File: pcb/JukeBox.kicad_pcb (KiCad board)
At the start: 2 copper layers, 102 x 100 mm, 102 parts, among them J1 USB_C_Receptacle_USB2.0_16P, Q1 Q_NPN_BEC, SW1 SW_SPST, SW10 SW_SPST, SW11 SW_SPST, SW12 SW_SPST, SW2 SW_SPST, SW3 SW_SPST, SW4 SW_SPST, SW5 SW_SPST, SW6 SW_SPST, SW7 SW_SPST, SW8 SW_SPST, SW9 SW_SPST, U1 NCP1117-3.3_SOT223, U2 W25Q128JVS, U3 RP2350_60QFN, U5 CAT24C512, Y2 ABM8-272-T3

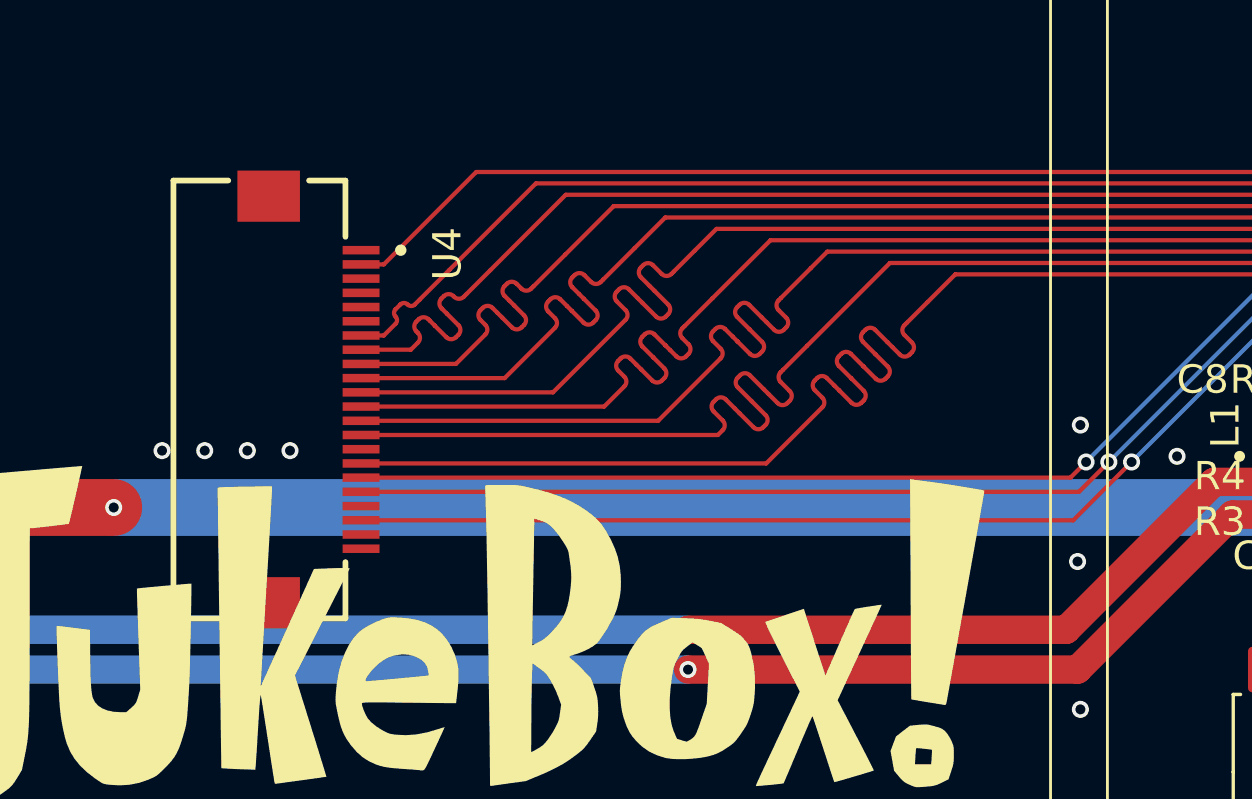
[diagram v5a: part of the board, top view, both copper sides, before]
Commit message: update to new part on pcb for screen
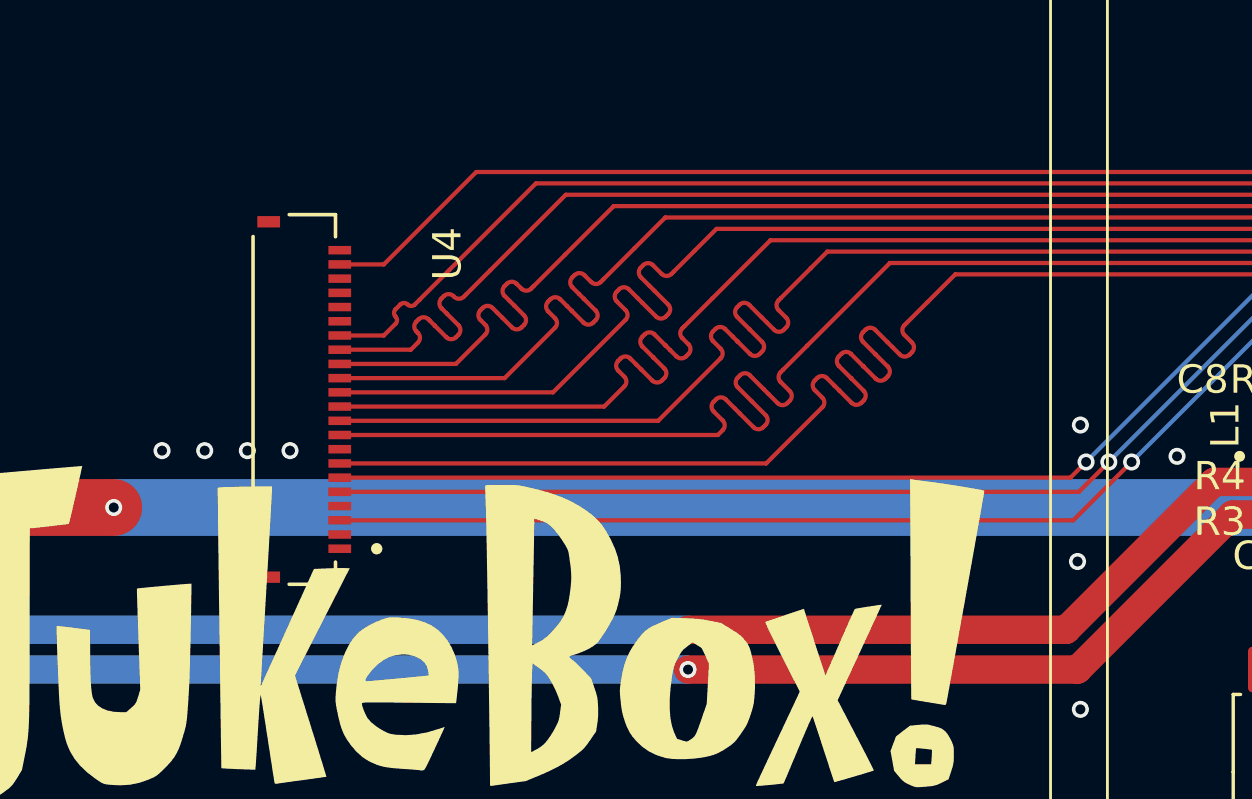
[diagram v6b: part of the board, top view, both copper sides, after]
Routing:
- net /SCRD3: track 54.9 -> 55.7 mm
- net /SCRRST: track 64.9 -> 65.7 mm
- net /SCRDC: track 66.4 -> 67.2 mm
- net /SCRD7: track 55.0 -> 55.7 mm
- net /SCRD6: track 54.9 -> 55.7 mm
- net /SCRD5: track 54.9 -> 55.7 mm
- net /SCRD2: track 54.9 -> 55.7 mm
- net /SCRD1: track 54.9 -> 55.7 mm
- net /SCRD0: track 54.9 -> 55.7 mm
- net /SCRCS: track 66.9 -> 67.7 mm
- net /SCRCLK: track 54.9 -> 55.6 mm
- net /LEDK: track 55.5 -> 56.2 mm
- net /SCRD4: track 54.9 -> 55.7 mm

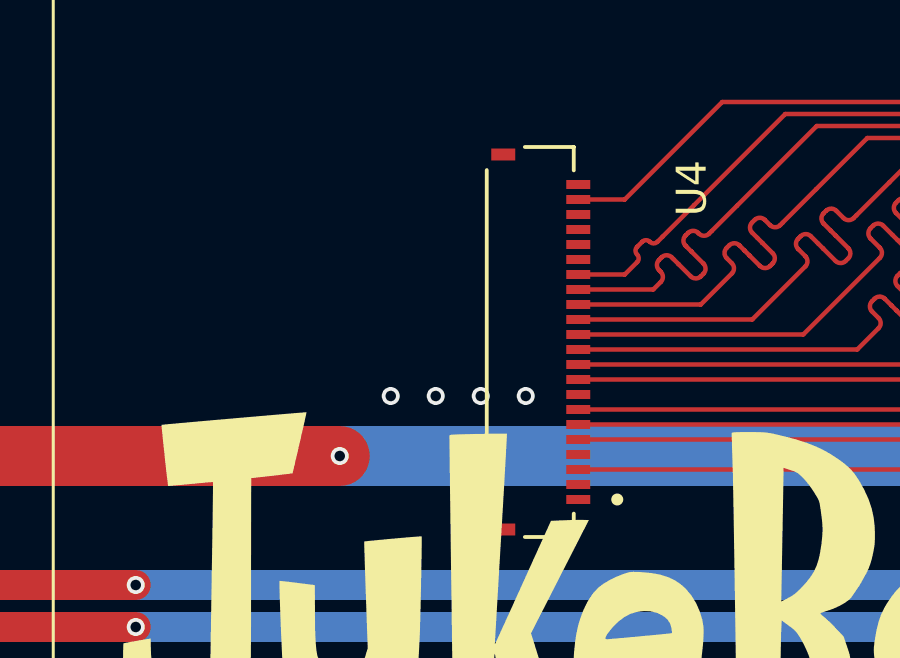
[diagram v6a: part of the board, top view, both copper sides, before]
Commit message: finalize power rails for new screen
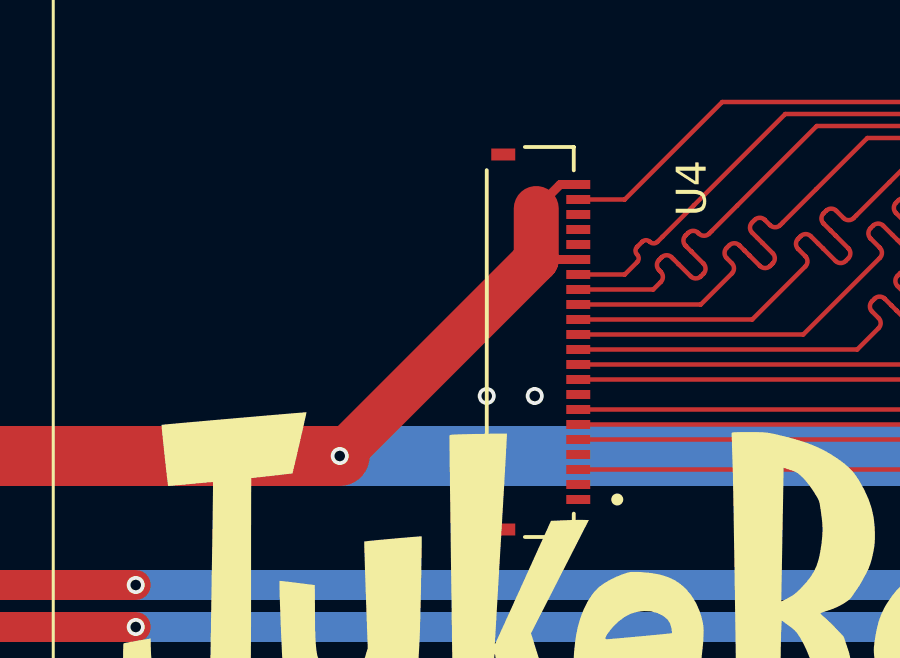
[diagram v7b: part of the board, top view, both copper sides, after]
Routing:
- net +3V3: track 149.5 -> 163.6 mm
- net GND: vias 57 -> 55
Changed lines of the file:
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@@
 	)
 	(via
-		(at 107.09 85.5)
+		(at 107.39 85.5)
 		(size 0.6)
 		(drill 0.35)
@@
 	)
 	(via
-		(at 102.59 85.5)
-		(size 0.6)
-		(drill 0.35)
-		(layers "F.Cu" "B.Cu")
-		(free yes)
-		(net 1)
-	)
-	(via
 		(at 155.19 84.6)
 		(size 0.6)
@@
 	)
 	(via
-		(at 104.09 85.5)
-		(size 0.6)
-		(drill 0.35)
-		(layers "F.Cu" "B.Cu")
-		(free yes)
-		(net 1)
-	)
-	(via
 		(at 148.09 79.5)
 		(size 0.6)
@@
 	)
 	(via
-		(at 105.59 85.5)
+		(at 105.79 85.5)
 		(size 0.6)
 		(drill 0.35)
@@
 	)
 	(segment
+		(start 108.24 78.45)
+		(end 108.84 78.45)
+		(width 0.3)
+		(layer "F.Cu")
+		(net 5)
+	)
+	(segment
+		(start 107.44 80.95)
+		(end 107.74 80.95)
+		(width 0.15)
+		(layer "F.Cu")
+		(net 5)
+	)
+	(segment
 		(start 144.27 88)
 		(end 144.47 88.2)
@@
 		(end 153.6275 85)
 		(width 0.15)
+		(layer "F.Cu")
+		(net 5)
+	)
+	(segment
+		(start 108.84 80.95)
+		(end 107.74 80.95)
+		(width 0.3)
 		(layer "F.Cu")
 		(net 5)
@@
 	)
 	(segment
+		(start 107.44 79.25)
+		(end 108.24 78.45)
+		(width 0.3)
+		(layer "F.Cu")
+		(net 5)
+	)
+	(segment
 		(start 150.19 84.3625)
 		(end 150.19 85)
@@
 	)
 	(segment
+		(start 100.89 87.5)
+		(end 107.44 80.95)
+		(width 1.5)
+		(layer "F.Cu")
+		(net 5)
+	)
+	(segment
 		(start 75.89 94.7)
 		(end 78.26 94.7)
@@
 		(layer "F.Cu")
 		(net 5)
+	)
+	(segment
+		(start 107.44 80.95)
+		(end 107.44 79.25)
+		(width 1.5)
+		(layer "F.Cu")
+		(net 5)

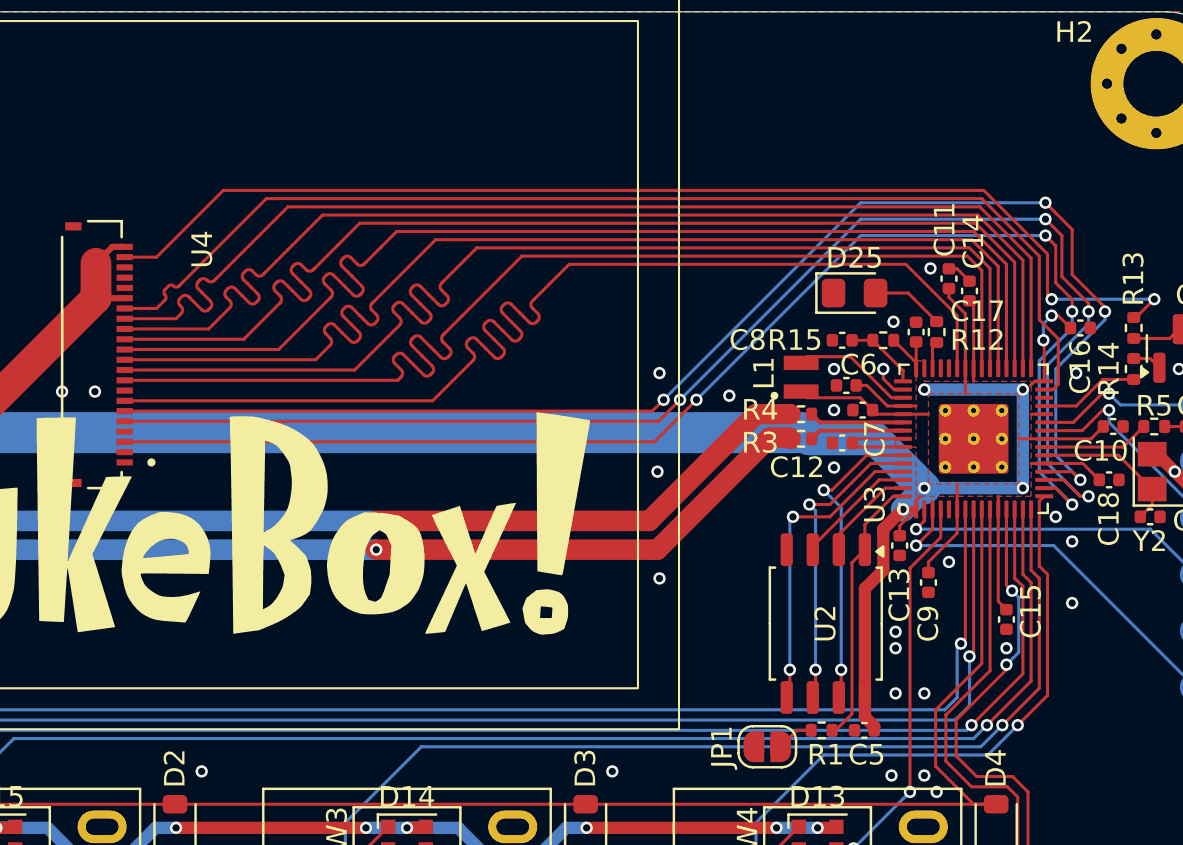
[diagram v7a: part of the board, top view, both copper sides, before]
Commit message: reorder screen pins (will make programming later easier)
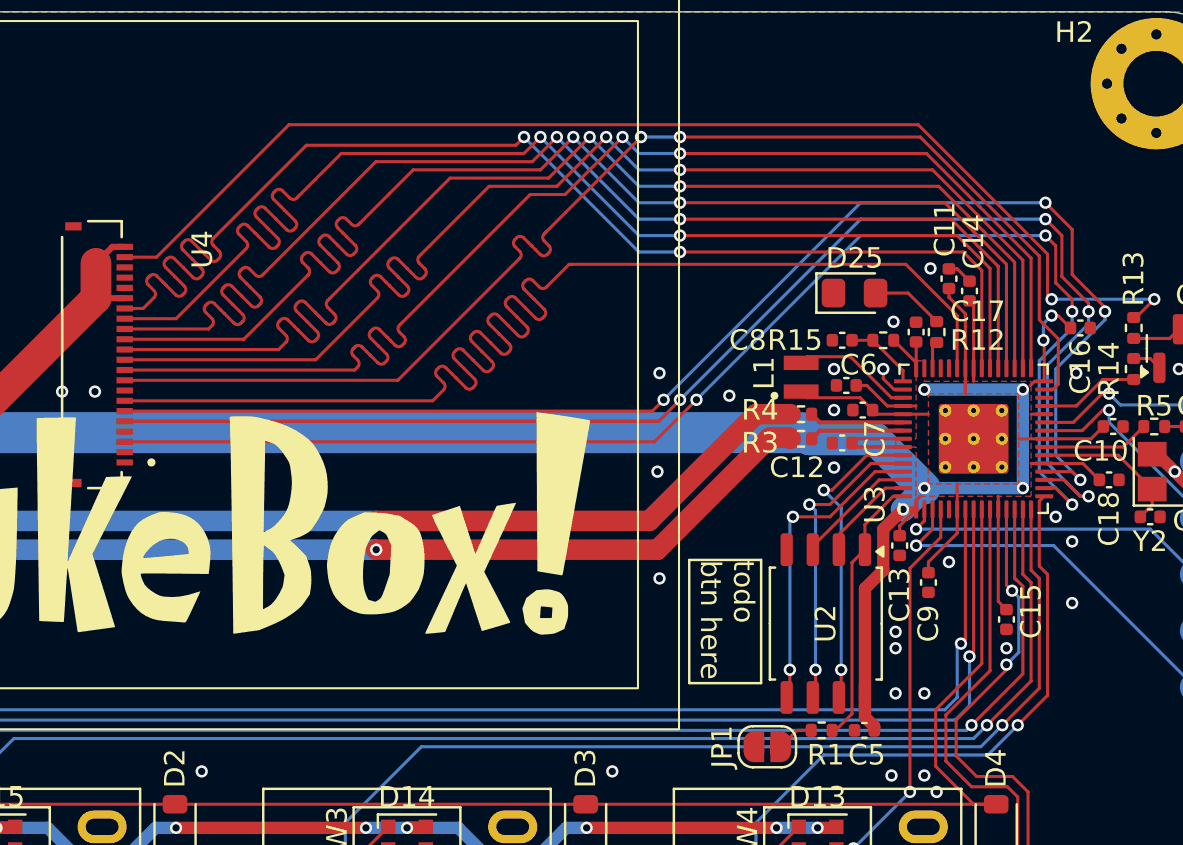
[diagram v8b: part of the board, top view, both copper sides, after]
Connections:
- U3 pad 29: /SCRD7 -> /SCRD0
- U3 pad 31: /SCRD6 -> /SCRD1
- U3 pad 32: /SCRD5 -> /SCRD2
- U3 pad 33: /SCRD4 -> /SCRD3
- U3 pad 34: /SCRD3 -> /SCRD4
- U3 pad 35: /SCRD2 -> /SCRD5
- U3 pad 36: /SCRD1 -> /SCRD6
- U3 pad 37: /SCRD0 -> /SCRD7
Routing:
- net /SCRCLK: track 55.6 -> 64.8 mm
- net /SCRD0: track 55.7 -> 61.9 mm, vias 0 -> 2
- net /SCRD2: track 55.7 -> 61.8 mm, vias 0 -> 2
- net /SCRD1: track 55.7 -> 61.8 mm, vias 0 -> 2
- net /SCRD3: track 55.7 -> 61.8 mm, vias 0 -> 2
- net /SCRD6: track 55.7 -> 61.8 mm, vias 0 -> 2
- net /SCRD4: track 55.7 -> 61.8 mm, vias 0 -> 2
- net /SCRD5: track 55.7 -> 61.8 mm, vias 0 -> 2
- net /SCRD7: track 55.7 -> 61.8 mm, vias 0 -> 2
- net /LEDK: track 56.2 -> 58.9 mm
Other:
- board text added: "todo btn here"
